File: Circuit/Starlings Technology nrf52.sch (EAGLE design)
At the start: 58 parts, among them J4 USB Micro, J7 CORTEX_DEBUG_SMD, Q2 BSS84, U2 MCP73831, U3 BC840M, U4 MIC5317 (MIC5205), U5 74AHCT2G125, U8 TPS61235P, Y2 FC-12M

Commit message: Adding new rocker switch and two tactile switches. Footprints are drawn and ready, just needs routing.
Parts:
- removed S3: (no value), SparkFun-Switches:SWITCH-SPDT-SMD-RIGHT-ANGLE
- removed S4: (no value), SparkFun-Switches:SWITCH-SPDT-PTH-11.6X4.0MM
- removed TP3: TPSB1,27, testpad:TPSB1,27
- added J8: (no value), SparkFun-Connectors:CONN_01
- added SW1, SW2: FSM8JSMASTR, FSM8JSMASTR:FSM8JSMASTR
- S1: value SPST-SMD-5.2MM -> CF-LD-1DC4-AR2W; device SparkFun-Switches:MOMENTARY-SWITCH-SPST-SMD-5.2MM -> RA1122DWR:CF-LD-1DC4-AR2W; DIGIKEY CKN12222-1-ND -> (none)
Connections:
- new net SWITCH_2: SW2.3, SW2.4
- net GND: now also SW1.1, SW1.2, SW2.1, SW2.2; no longer S1.1
- net SWITCH_1: now also SW1.3, SW1.4; no longer S1.2
- net VBAT: now also J8.1, S1.4; no longer S3.O, S4.O
- net VBAT_RAW: now also S1.5; no longer S3.P, S4.P, TP3.PP
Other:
- note added: "Input is 3V3 from nrf52 Output is to 5V leds"
- note removed: "Input is 5V from nrf52 Output is to 3V3 leds"

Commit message: Adding digikey part number for rocker switch.
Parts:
- S1: DIGIKEY (none) -> 563-1946-ND
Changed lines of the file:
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@@
 <part name="SW2" library="FSM8JSMASTR" deviceset="FSM8JSMASTR" device=""/>
 <part name="J8" library="SparkFun-Connectors" library_urn="urn:adsk.eagle:library:513" deviceset="CONN_01" device="" package3d_urn="urn:adsk.eagle:package:38028/1"/>
-<part name="S1" library="RA1122DWR" deviceset="CF-LD-1DC4-AR2W" device=""/>
+<part name="S1" library="RA1122DWR" deviceset="CF-LD-1DC4-AR2W" device="">
+<attribute name="DIGIKEY" value="563-1946-ND"/>
+</part>
 </parts>
 <sheets>
@@
 <instance part="S1" gate="A" x="454.66" y="160.02" smashed="yes">
 <attribute name="NAME" x="447.04" y="162.56" size="1.27" layer="95"/>
+<attribute name="DIGIKEY" x="454.66" y="160.02" size="1.778" layer="96" display="off"/>
 </instance>
 </instances>

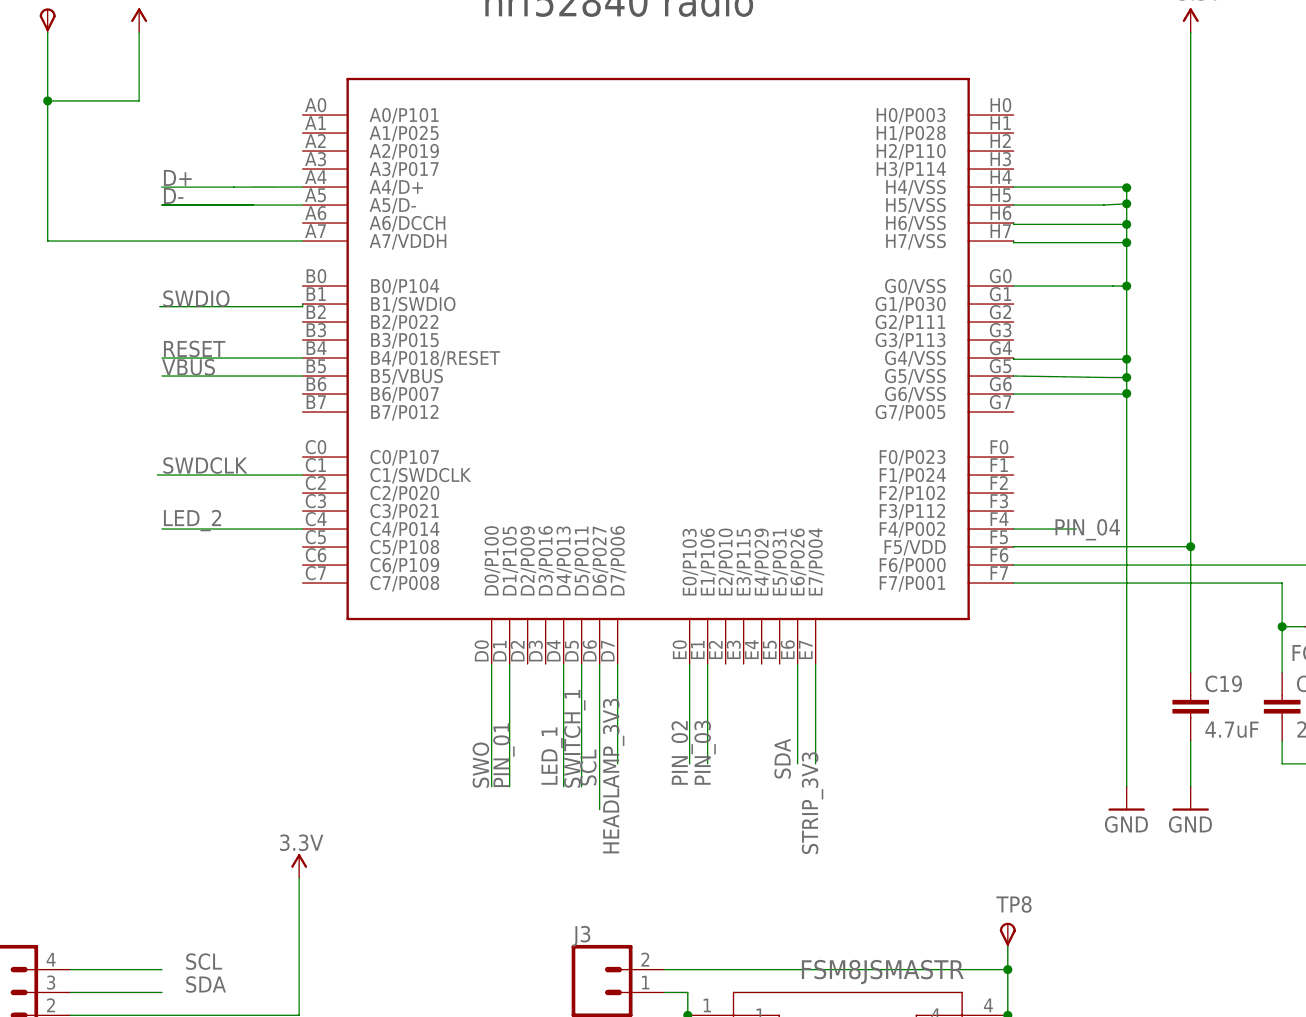
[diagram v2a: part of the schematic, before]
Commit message: Adjusting dimensions, adding pins to expansion header, connecting second switch.
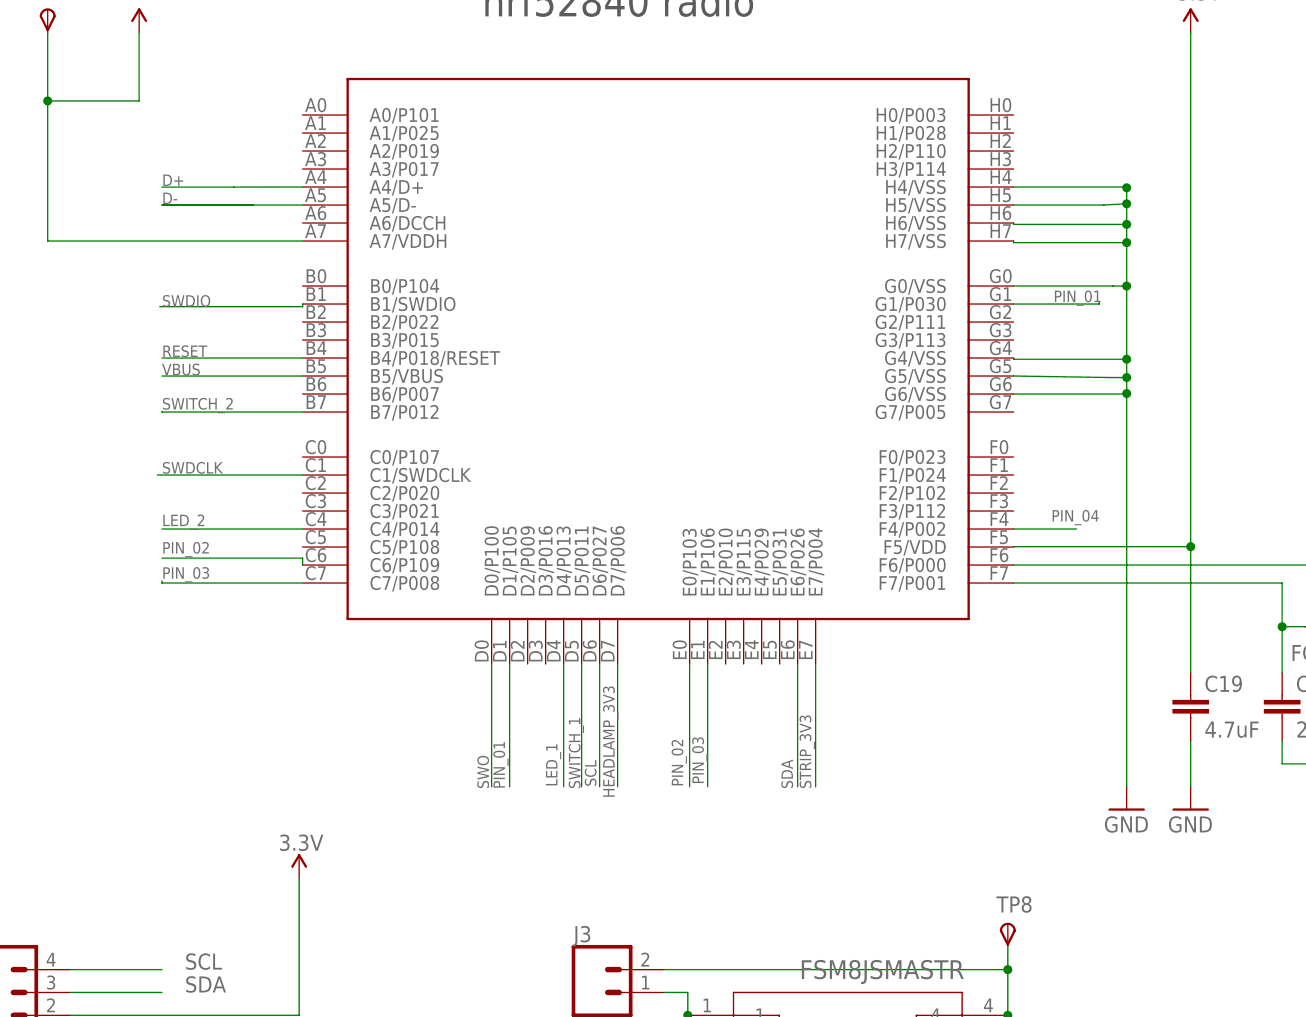
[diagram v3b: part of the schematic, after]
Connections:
- net PIN_01: now also U3.G1/P030
- net PIN_02: now also U3.C6/P109
- net PIN_03: now also U3.C7/P008
- net SWITCH_2: now also U3.B7/P012
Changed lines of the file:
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@@
 <pinref part="U3" gate="G$1" pin="B4/P018/RESET"/>
 <wire x1="46.106" y1="131.454" x2="30.48" y2="131.454" width="0.1524" layer="91"/>
-<label x="30.48" y="131.572" size="1.778" layer="95"/>
+<label x="30.48" y="131.572" size="1.27" layer="95"/>
 </segment>
 <segment>
@@
 <wire x1="46.106" y1="148.454" x2="30.48" y2="148.454" width="0.1524" layer="91"/>
 <wire x1="30.48" y1="148.454" x2="40.64" y2="148.463" width="0.1524" layer="91"/>
-<label x="30.48" y="148.5646" size="1.778" layer="95"/>
+<label x="30.48" y="148.5646" size="1.27" layer="95"/>
 </segment>
 <segment>
@@
 <wire x1="30.4546" y1="150.4442" x2="38.4606" y2="150.4442" width="0.1524" layer="91"/>
 <wire x1="38.4606" y1="150.4442" x2="46.106" y2="150.454" width="0.1524" layer="91"/>
-<label x="30.48" y="150.5712" size="1.778" layer="95"/>
+<label x="30.48" y="150.5712" size="1.27" layer="95"/>
 </segment>
 <segment>
@@
 <pinref part="U3" gate="G$1" pin="C1/SWDCLK"/>
 <wire x1="46.106" y1="118.454" x2="29.972" y2="118.454" width="0.1524" layer="91"/>
-<label x="30.48" y="118.618" size="1.778" layer="95"/>
+<label x="30.48" y="118.618" size="1.27" layer="95"/>
 </segment>
 <segment>
@@
 <wire x1="46.106" y1="137.454" x2="46.106" y2="137.16" width="0.1524" layer="91"/>
 <wire x1="46.106" y1="137.16" x2="30.226" y2="137.16" width="0.1524" layer="91"/>
-<label x="30.48" y="137.16" size="1.778" layer="95"/>
+<label x="30.48" y="137.16" size="1.27" layer="95"/>
 </segment>
 <segment>
@@
 <pinref part="U3" gate="G$1" pin="D0/P100"/>
 <wire x1="67.106" y1="97.454" x2="67.106" y2="83.82" width="0.1524" layer="91"/>
-<label x="66.802" y="83.566" size="1.778" layer="95" rot="R90"/>
+<label x="66.802" y="83.566" size="1.27" layer="95" rot="R90"/>
 </segment>
 </net>
@@
 <segment>
 <pinref part="U3" gate="G$1" pin="E7/P004"/>
-<wire x1="103.106" y1="97.454" x2="103.106" y2="86.36" width="0.1524" layer="91"/>
-<label x="103.378" y="76.2" size="1.778" layer="95" rot="R90"/>
+<wire x1="103.106" y1="97.454" x2="103.106" y2="83.82" width="0.1524" layer="91"/>
+<label x="102.616" y="83.566" size="1.27" layer="95" rot="R90"/>
 </segment>
 </net>
@@
 <pinref part="U3" gate="G$1" pin="D5/P011"/>
 <wire x1="77.106" y1="97.454" x2="77.106" y2="83.82" width="0.1524" layer="91"/>
-<label x="76.962" y="83.566" size="1.778" layer="95" rot="R90"/>
+<label x="76.962" y="83.566" size="1.27" layer="95" rot="R90"/>
 </segment>
 </net>
@@
 <pinref part="U3" gate="G$1" pin="C4/P014"/>
 <wire x1="46.106" y1="112.454" x2="30.48" y2="112.454" width="0.1524" layer="91"/>
-<label x="30.48" y="112.776" size="1.778" layer="95"/>
+<label x="30.48" y="112.776" size="1.27" layer="95"/>
 </segment>
 </net>
@@
 <pinref part="U3" gate="G$1" pin="B5/VBUS"/>
 <wire x1="46.106" y1="129.454" x2="30.48" y2="129.454" width="0.1524" layer="91"/>
-<label x="30.48" y="129.54" size="1.778" layer="95"/>
+<label x="30.48" y="129.54" size="1.27" layer="95"/>
 </segment>
 <segment>
@@
 <segment>
 <pinref part="U3" gate="G$1" pin="D7/P006"/>
-<wire x1="81.106" y1="97.454" x2="81.106" y2="86.36" width="0.1524" layer="91"/>
-<label x="81.28" y="76.2" size="1.778" layer="95" rot="R90"/>
+<wire x1="81.106" y1="97.454" x2="81.106" y2="83.82" width="0.1524" layer="91"/>
+<label x="80.772" y="82.55" size="1.27" layer="95" rot="R90"/>
 </segment>
 <segment>
@@
 <segment>
 <pinref part="U3" gate="G$1" pin="E6/P026"/>
-<wire x1="101.106" y1="97.454" x2="101.106" y2="86.36" width="0.1524" layer="91"/>
-<label x="100.33" y="84.582" size="1.778" layer="95" rot="R90"/>
+<wire x1="101.106" y1="97.454" x2="101.106" y2="83.82" width="0.1524" layer="91"/>
+<label x="100.584" y="83.566" size="1.27" layer="95" rot="R90"/>
 </segment>
 </net>
@@
 <segment>
 <pinref part="U3" gate="G$1" pin="D6/P027"/>
-<wire x1="79.106" y1="97.454" x2="79.106" y2="81.28" width="0.1524" layer="91"/>
-<label x="78.74" y="83.82" size="1.778" layer="95" rot="R90"/>
+<wire x1="79.106" y1="97.454" x2="79.106" y2="83.82" width="0.1524" layer="91"/>
+<label x="78.74" y="83.82" size="1.27" layer="95" rot="R90"/>
 </segment>
 </net>
@@
 <pinref part="U3" gate="G$1" pin="D1/P105"/>
 <wire x1="69.106" y1="97.454" x2="69.106" y2="83.82" width="0.1524" layer="91"/>
-<label x="69.088" y="83.566" size="1.778" layer="95" rot="R90"/>
+<label x="68.58" y="83.566" size="1.27" layer="95" rot="R90"/>
+</segment>
+<segment>
+<pinref part="U3" gate="G$1" pin="G1/P030"/>
+<wire x1="125.106" y1="137.454" x2="134.62" y2="137.454" width="0.1524" layer="91"/>
+<wire x1="134.62" y1="137.454" x2="134.62" y2="137.668" width="0.1524" layer="91"/>
+<label x="129.54" y="137.668" size="1.27" layer="95"/>
 </segment>
 </net>
@@
 <segment>
 <pinref part="U3" gate="G$1" pin="E0/P103"/>
-<wire x1="89.106" y1="97.454" x2="89.106" y2="86.36" width="0.1524" layer="91"/>
-<label x="88.9" y="83.82" size="1.778" layer="95" rot="R90"/>
+<wire x1="89.106" y1="97.454" x2="89.106" y2="83.82" width="0.1524" layer="91"/>
+<label x="88.392" y="83.82" size="1.27" layer="95" rot="R90"/>
+</segment>
+<segment>
+<pinref part="U3" gate="G$1" pin="C6/P109"/>
+<wire x1="46.106" y1="108.454" x2="46.106" y2="109.22" width="0.1524" layer="91"/>
+<wire x1="46.106" y1="109.22" x2="30.48" y2="109.22" width="0.1524" layer="91"/>
+<label x="30.48" y="109.728" size="1.27" layer="95"/>
 </segment>
 </net>
@@
 <segment>
 <pinref part="U3" gate="G$1" pin="E1/P106"/>
-<wire x1="91.106" y1="97.454" x2="91.106" y2="86.36" width="0.1524" layer="91"/>
-<label x="91.44" y="83.82" size="1.778" layer="95" rot="R90"/>
+<wire x1="91.106" y1="97.454" x2="91.106" y2="83.82" width="0.1524" layer="91"/>
+<label x="90.678" y="84.074" size="1.27" layer="95" rot="R90"/>
+</segment>
+<segment>
+<pinref part="U3" gate="G$1" pin="C7/P008"/>
+<wire x1="46.106" y1="106.454" x2="30.48" y2="106.454" width="0.1524" layer="91"/>
+<wire x1="30.48" y1="106.454" x2="30.48" y2="106.68" width="0.1524" layer="91"/>
+<label x="30.48" y="106.934" size="1.27" layer="95"/>
 </segment>
 </net>
@@
 <pinref part="U3" gate="G$1" pin="F4/P002"/>
 <wire x1="125.106" y1="112.454" x2="132.08" y2="112.454" width="0.1524" layer="91"/>
-<label x="129.54" y="111.76" size="1.778" layer="95"/>
+<label x="129.286" y="113.284" size="1.27" layer="95"/>
 </segment>
 </net>
@@
 <pinref part="U3" gate="G$1" pin="D4/P013"/>
 <wire x1="75.106" y1="97.454" x2="75.106" y2="83.82" width="0.1524" layer="91"/>
-<label x="74.422" y="83.82" size="1.778" layer="95" rot="R90"/>
+<label x="74.422" y="83.82" size="1.27" layer="95" rot="R90"/>
 </segment>
 </net>
@@
 <label x="134.62" y="33.02" size="1.778" layer="95" xref="yes"/>
 </segment>
-</net>
+<segment>
+<pinref part="U3" gate="G$1" pin="B7/P012"/>
+<wire x1="46.106" y1="125.454" x2="30.48" y2="125.454" width="0.1524" layer="91"/>
+<wire x1="30.48" y1="125.454" x2="30.48" y2="125.476" width="0.1524" layer="91"/>
+<label x="30.48" y="125.73" size="1.27" layer="95"/>
+</segment>
+</net>

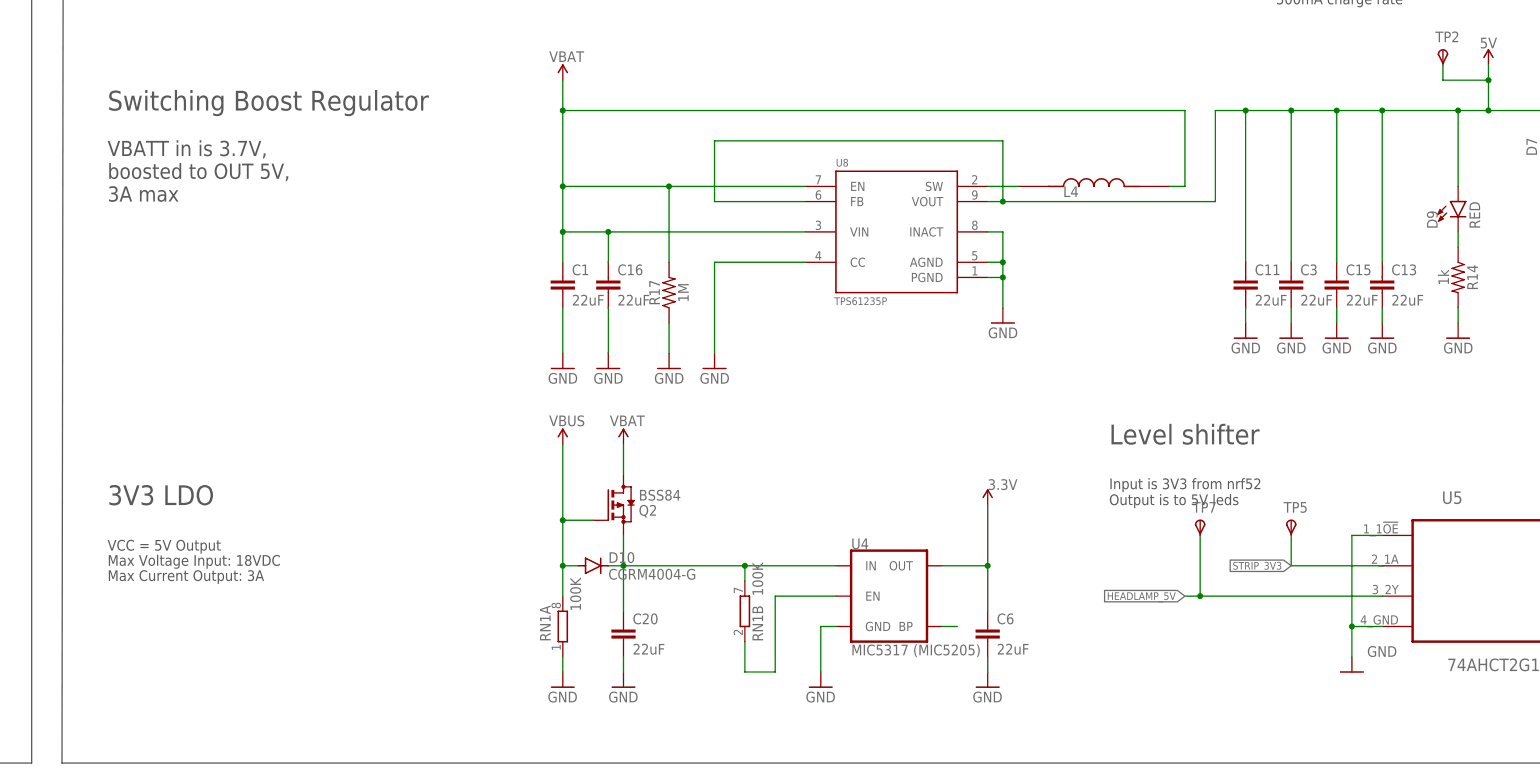
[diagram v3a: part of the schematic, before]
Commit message: Revision 10
- Adding second tactile switch
- Adjusting board dimensions to place buttons
- Adding rocker on/off switch
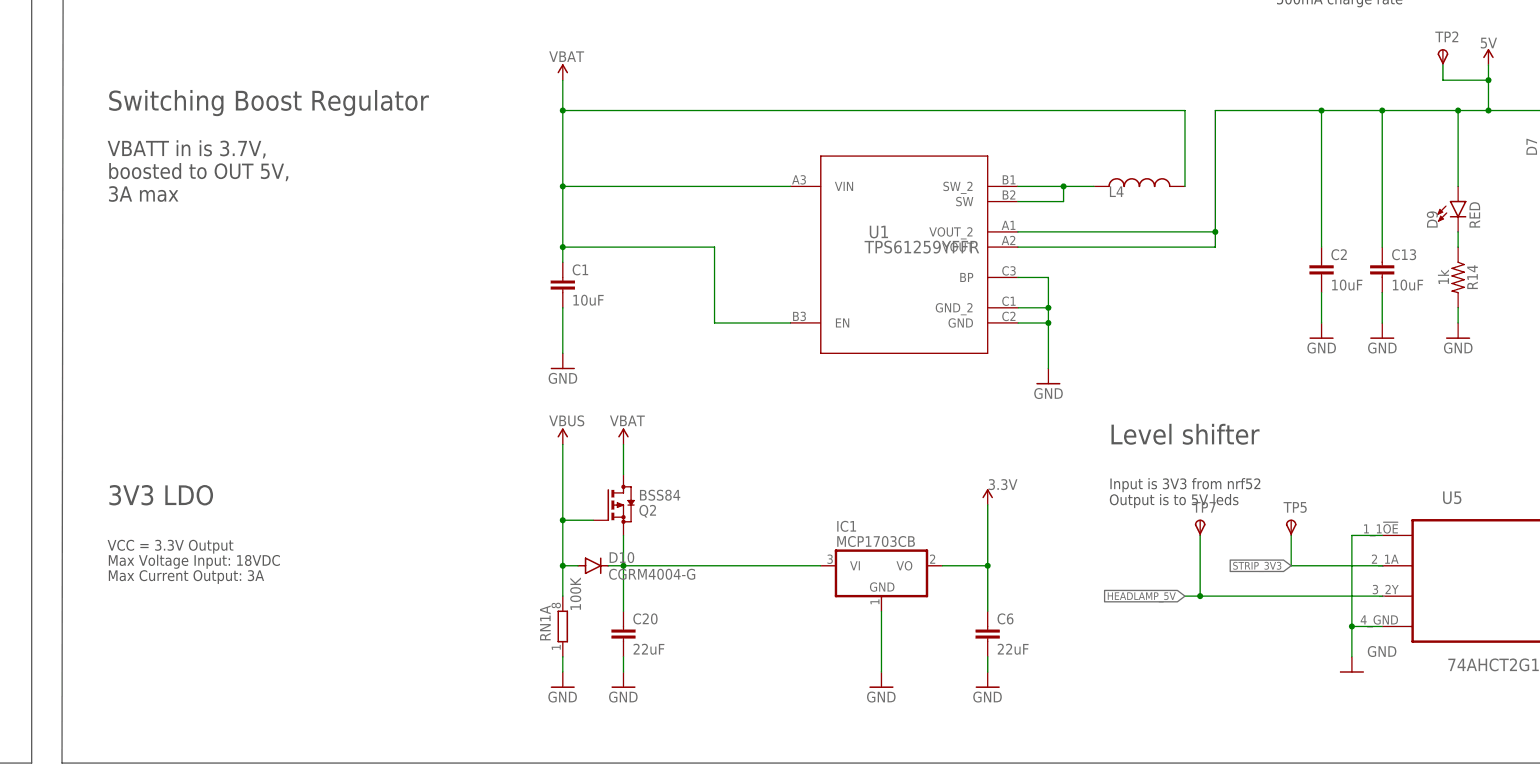
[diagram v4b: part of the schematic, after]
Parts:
- removed C11, C15, C16, C3: 22uF, SparkFun-Capacitors:22UF-0805-6.3V-20%
- removed R17: 1M, SparkFun-Resistors:750KOHM-0603-1/10W-1%
- removed U4: MIC5317 (MIC5205), SparkFun-IC-Power:V_REG_MIC52053.3V
- removed U8: TPS61235P, TPS61235PRWLR:TPS61235PRWLR
- added C2: 10uF, SparkFun-Capacitors:10UF-0603-6.3V-20%
- added IC1: MCP1703CB, linear:MCP1703CB
- added U1: TPS61259YFFR, TPS6125x:TPS61259YFFR
- C1, C13: value 22uF -> 10uF; device SparkFun-Capacitors:22UF-0805-6.3V-20% -> SparkFun-Capacitors:10UF-0603-6.3V-20%; DIGIKEY 490-10511-1-ND -> 587-1256-1-ND
- D10: DIGIKEY MBR120LSFT3GOSTR-ND -> 3757-SBA130AS_R1_00001TR-ND
- D7, D8: DIGIKEY B240AE-13DITR-ND -> 3757-SBA130AS_R1_00001TR-ND
- L4: device FDSD0630-H-1R0M_P3:FDSD0630-H-1R0M=P3 -> 1277AS-H-1R0M_P2:1277AS-H-1R0M=P2; DIGIKEY 490-10878-1-ND -> 490-10590-2-ND
- Q2: DIGIKEY TSM2305CXRFGTR-ND -> DMG2301L-7DITR-ND
- SW1, SW2: DIGIKEY (none) -> 450-2135-2-ND
- U2: DIGIKEY MCP73832T-2DFI/OTTR-ND -> MCP73831T-2ACI/OTTR-ND
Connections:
- removed net N$5: RN1B.1, U4.EN
- removed net N$6: U4.BP
- net 3.3V: now also IC1.VO; no longer U4.OUT
- net 5V: now also C2.1, U1.VOUT, U1.VOUT_2; no longer C11.1, C15.1, C3.1, U8.FB, U8.VOUT
- net GND: now also C2.2, IC1.GND, U1.BP, U1.GND, U1.GND_2; no longer C11.2, C15.2, C16.2, C3.2, R17.1, U4.GND, U8.AGND, U8.CC, U8.INACT, U8.PGND
- net N$3: now also U1.SW, U1.SW_2; no longer U8.SW
- net N$4: now also IC1.VI; no longer RN1B.2, U4.IN
- net VBAT: now also U1.EN, U1.VIN; no longer C16.1, R17.2, U8.EN, U8.VIN
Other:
- note added: "Revision history: 2022-03-11: Revision 10 - Adding second tactile switch - Adjusting board dimensions to place buttons - Adding rocker on/off switch 2021-06-24: Revision 9 - Moving to nrf52840-DK BSP pins for buttons and leds - Driving LEDs with active LOW - Adding debugging pins for switch and leds 2021-05-24: Revision 8 - Fixed footprint of level shifter, XTAL, and connectors - Updated DigiKey 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"
- note added: "VCC = 3.3V Output"
- note removed: "Revision history: 2021-06-24: Revision 9 - Moving to nrf52840-DK BSP pins for buttons and leds - Driving LEDs with active LOW - Adding debugging pins for switch and leds 2021-05-24: Revision 8 - Fixed footprint of level shifter, XTAL, and connectors - Updated DigiKey part numbers - Swapped adjustable boost converter for fixed - Headlamp to P0.06 - Switch to P0.30 2021-03-12: Revision 7 - Connecto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"
- note removed: "VCC = 5V Output"
- moved on the sheet: C13
